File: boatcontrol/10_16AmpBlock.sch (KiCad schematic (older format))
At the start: 15 parts, among them U6101 ULN2803A

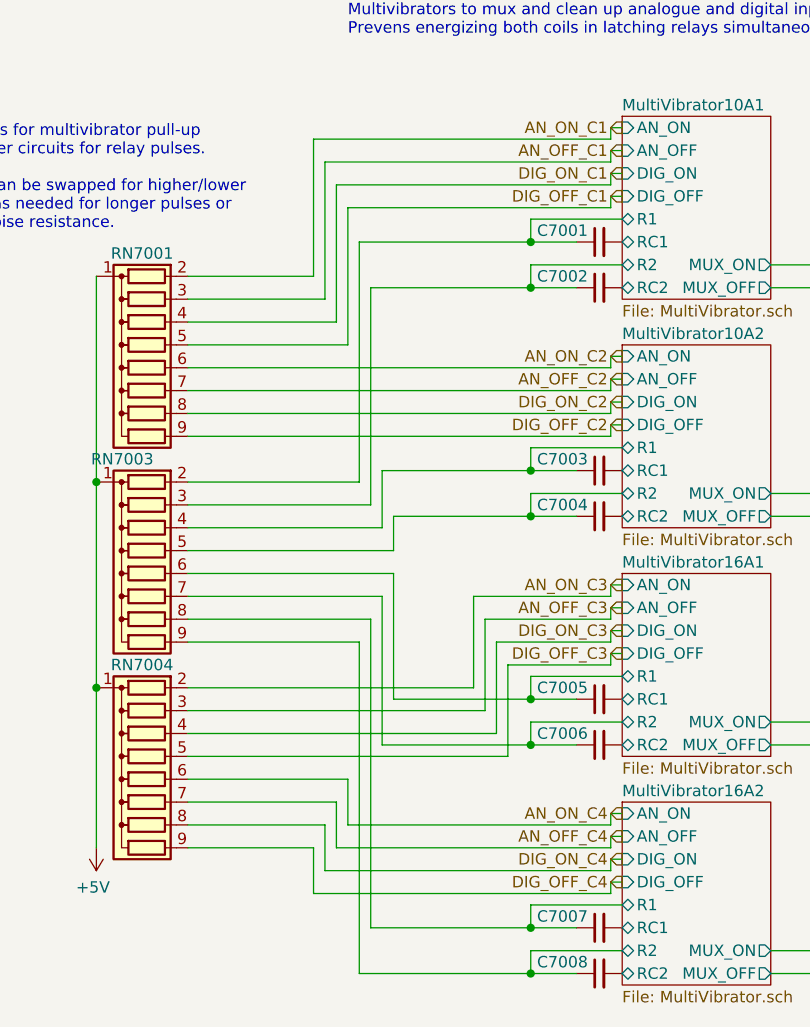
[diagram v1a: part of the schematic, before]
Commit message: Rewiring resistors done
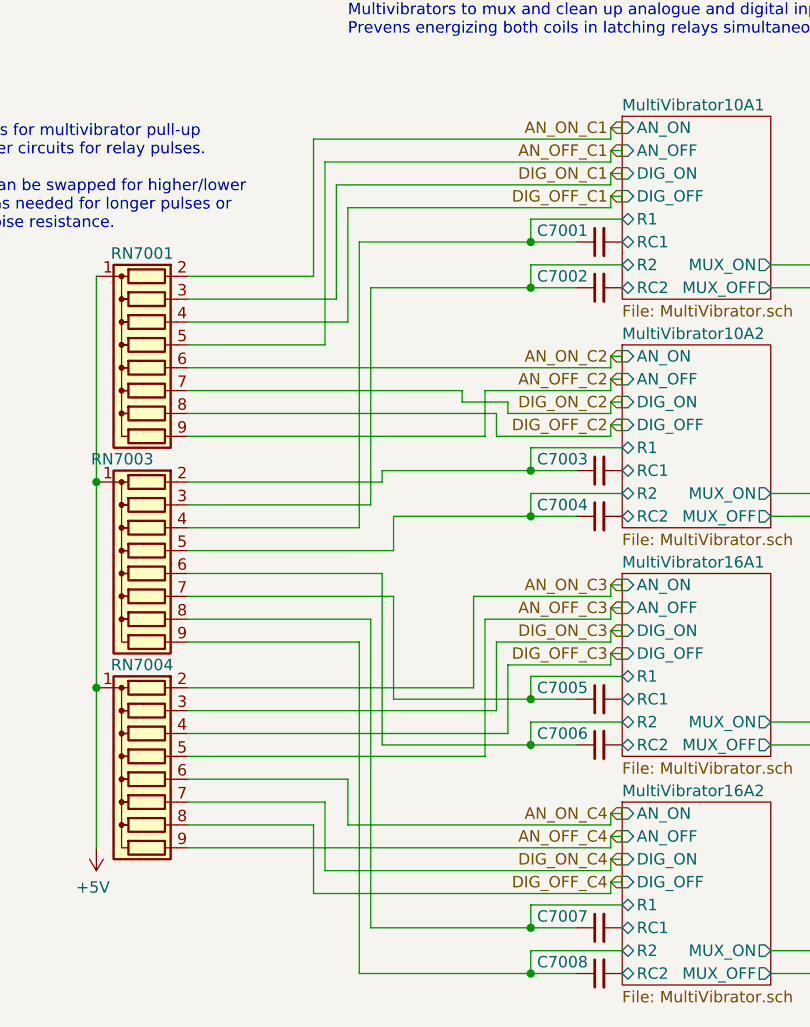
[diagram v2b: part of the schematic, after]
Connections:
- net AN_OFF_C1: now also RN6101.5 (R4); no longer RN6101.3 (R2)
- net AN_OFF_C2: now also RN6101.9 (R8); no longer RN6101.7 (R6)
- net AN_OFF_C3: now also RN6104.5 (R4); no longer RN6104.3 (R2)
- net AN_OFF_C4: now also RN6104.9 (R8); no longer RN6104.7 (R6)
- net DIG_OFF_C1: now also RN6101.4 (R3); no longer RN6101.5 (R4)
- net DIG_OFF_C2: now also RN6101.8 (R7); no longer RN6101.9 (R8)
- net DIG_OFF_C3: now also RN6104.4 (R3); no longer RN6104.5 (R4)
- net DIG_OFF_C4: now also RN6104.8 (R7); no longer RN6104.9 (R8)
- net DIG_ON_C1: now also RN6101.3 (R2); no longer RN6101.4 (R3)
- net DIG_ON_C2: now also RN6101.7 (R6); no longer RN6101.8 (R7)
- net DIG_ON_C3: now also RN6104.3 (R2); no longer RN6104.4 (R3)
- net DIG_ON_C4: now also RN6104.7 (R6); no longer RN6104.8 (R7)
- net MultiVibrator10A1/R1: now also RN7003.4 (R3); no longer RN7003.2 (R1)
- net MultiVibrator10A2/R1: now also RN7003.2 (R1); no longer RN7003.4 (R3)
- net MultiVibrator16A1/R1: now also RN7003.7 (R6); no longer RN7003.6 (R5)
- net MultiVibrator16A1/R2: now also RN7003.6 (R5); no longer RN7003.7 (R6)

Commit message: mwire
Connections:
- net 10AC1/OFF_COIL: now also RN6102.10 (R7.2); no longer RN6102.9 (R8.2)
- net 10AC1/ON_COIL: now also RN6102.9 (R8.2); no longer RN6102.10 (R7.2)
- net 10AC2/OFF_COIL: now also RN6102.12 (R5.2); no longer RN6102.11 (R6.2)
- net 10AC2/ON_COIL: now also RN6102.11 (R6.2); no longer RN6102.12 (R5.2)
- net 16AC1/OFF_COIL: now also RN6102.14 (R3.2); no longer RN6102.13 (R4.2)
- net 16AC1/ON_COIL: now also RN6102.13 (R4.2); no longer RN6102.14 (R3.2)
- net 16AC2/OFF_COIL: now also RN6102.16 (R1.2); no longer RN6102.15 (R2.2)
- net 16AC2/ON_COIL: now also RN6102.15 (R2.2); no longer RN6102.16 (R1.2)
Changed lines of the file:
@@
 $Descr A4 11693 8268
 encoding utf-8
-Sheet 69 97
+Sheet 49 97
 Title "Boat Control Hat"
 Date "2020-07-09"
@@
 AR Path="/D1BB8DB4/5F76AF55/604747AF" Ref="U6101"  Part="1"
 AR Path="/D1BB8DB4/5F75E923/604747AF" Ref="U7001"  Part="1"
-F 0 "U7001" H 6450 3500 50  0000 L CNN
+F 0 "U6101" H 6450 3500 50  0000 L CNN
 F 1 "ULN2803A" H 6300 4200 50  0000 L CNN
 F 2 "Package_DIP:DIP-18_W7.62mm" H 6550 3050 50  0001 L CNN
@@
 AR Path="/D1BB8DB4/5F76AF55/60474926" Ref="RN6102"  Part="1"
 AR Path="/D1BB8DB4/5F75E923/60474926" Ref="RN7002"  Part="1"
-F 0 "RN7002" V 10200 4350 50  0000 L CNN
+F 0 "RN6102" V 10200 4350 50  0000 L CNN
 F 1 "680Ω" V 9800 3750 50  0001 L CNN
 F 2 "BoatControl:DIP254P762X432-16P" V 10775 3900 50  0001 C CNN
@@
 AR Path="/D1BB8DB4/5F75E923/62B5C7B5" Ref="C7001"  Part="1"
 AR Path="/D1BB8DB4/5F76AF55/62B5C7B5" Ref="C6101"  Part="1"
-F 0 "C7001" V 4600 2550 50  0000 L CNN
+F 0 "C6101" V 4600 2550 50  0000 L CNN
 F 1 "1µF" H 3800 2400 50  0001 L CNN
 F 2 "Capacitor_THT:C_Disc_D7.5mm_W5.0mm_P5.00mm" H 4650 2500 50  0001 C CNN
@@
 AR Path="/D1BB8DB4/5F75E923/62B76848" Ref="C7002"  Part="1"
 AR Path="/D1BB8DB4/5F76AF55/62B76848" Ref="C6102"  Part="1"
-F 0 "C7002" V 4600 2750 50  0000 L CNN
+F 0 "C6102" V 4600 2750 50  0000 L CNN
 F 1 "1µF" H 3800 2600 50  0001 L CNN
 F 2 "Capacitor_THT:C_Disc_D7.5mm_W5.0mm_P5.00mm" H 4650 2700 50  0001 C CNN
@@
 AR Path="/D1BB8DB4/5F75E923/62B86A50" Ref="C7003"  Part="1"
 AR Path="/D1BB8DB4/5F76AF55/62B86A50" Ref="C6103"  Part="1"
-F 0 "C7003" V 4600 3550 50  0000 L CNN
+F 0 "C6103" V 4600 3550 50  0000 L CNN
 F 1 "1µF" H 3800 3400 50  0001 L CNN
 F 2 "Capacitor_THT:C_Disc_D7.5mm_W5.0mm_P5.00mm" H 4650 3500 50  0001 C CNN
@@
 AR Path="/D1BB8DB4/5F75E923/62B939DB" Ref="C7004"  Part="1"
 AR Path="/D1BB8DB4/5F76AF55/62B939DB" Ref="C6104"  Part="1"
-F 0 "C7004" V 4600 3750 50  0000 L CNN
+F 0 "C6104" V 4600 3750 50  0000 L CNN
 F 1 "1µF" H 3800 3600 50  0001 L CNN
 F 2 "Capacitor_THT:C_Disc_D7.5mm_W5.0mm_P5.00mm" H 4650 3700 50  0001 C CNN
@@
 AR Path="/D1BB8DB4/5F75E923/62BA14CE" Ref="C7005"  Part="1"
 AR Path="/D1BB8DB4/5F76AF55/62BA14CE" Ref="C6105"  Part="1"
-F 0 "C7005" V 4600 4550 50  0000 L CNN
+F 0 "C6105" V 4600 4550 50  0000 L CNN
 F 1 "1µF" H 3800 4400 50  0001 L CNN
 F 2 "Capacitor_THT:C_Disc_D7.5mm_W5.0mm_P5.00mm" H 4650 4500 50  0001 C CNN
@@
 AR Path="/D1BB8DB4/5F75E923/62BAE342" Ref="C7006"  Part="1"
 AR Path="/D1BB8DB4/5F76AF55/62BAE342" Ref="C6106"  Part="1"
-F 0 "C7006" V 4600 4750 50  0000 L CNN
+F 0 "C6106" V 4600 4750 50  0000 L CNN
 F 1 "1µF" H 3800 4600 50  0001 L CNN
 F 2 "Capacitor_THT:C_Disc_D7.5mm_W5.0mm_P5.00mm" H 4650 4700 50  0001 C CNN
@@
 AR Path="/D1BB8DB4/5F75E923/62BBBC28" Ref="C7007"  Part="1"
 AR Path="/D1BB8DB4/5F76AF55/62BBBC28" Ref="C6107"  Part="1"
-F 0 "C7007" V 4600 5550 50  0000 L CNN
+F 0 "C6107" V 4600 5550 50  0000 L CNN
 F 1 "1µF" H 3800 5400 50  0001 L CNN
 F 2 "Capacitor_THT:C_Disc_D7.5mm_W5.0mm_P5.00mm" H 4650 5500 50  0001 C CNN
@@
 AR Path="/D1BB8DB4/5F75E923/62BC8A92" Ref="C7008"  Part="1"
 AR Path="/D1BB8DB4/5F76AF55/62BC8A92" Ref="C6108"  Part="1"
-F 0 "C7008" V 4600 5750 50  0000 L CNN
+F 0 "C6108" V 4600 5750 50  0000 L CNN
 F 1 "1µF" H 3800 5600 50  0001 L CNN
 F 2 "Capacitor_THT:C_Disc_D7.5mm_W5.0mm_P5.00mm" H 4650 5700 50  0001 C CNN
@@
 AR Path="/D1BB8DB4/5F75E923/62CB5764" Ref="RN7003"  Part="1"
 AR Path="/D1BB8DB4/5F76AF55/62CB5764" Ref="RN6103"  Part="1"
-F 0 "RN7003" V 2150 3900 50  0000 L CNN
+F 0 "RN6103" V 2150 3900 50  0000 L CNN
 F 1 "10MΩ" H 2300 3550 50  0001 L CNN
 F 2 "Resistor_THT:R_Array_SIP9" V 3125 3950 50  0001 C CNN
@@
 AR Path="/D1BB8DB4/5F76AF55/630078FE" Ref="RN6101"  Part="1"
 AR Path="/D1BB8DB4/5F75E923/630078FE" Ref="RN7001"  Part="1"
-F 0 "RN7001" V 2150 3050 50  0000 C CNN
+F 0 "RN6101" V 2150 3050 50  0000 C CNN
 F 1 "100KΩ" V 2450 2750 50  0001 C CNN
 F 2 "Resistor_THT:R_Array_SIP9" H 3400 3150 50  0001 L CNN
@@
 AR Path="/D1BB8DB4/5F76AF55/63015012" Ref="RN6104"  Part="1"
 AR Path="/D1BB8DB4/5F75E923/63015012" Ref="RN7004"  Part="1"
-F 0 "RN7004" V 2150 4850 50  0000 C CNN
+F 0 "RN6104" V 2150 4850 50  0000 C CNN
 F 1 "100KΩ" V 2450 4550 50  0001 C CNN
 F 2 "Resistor_THT:R_Array_SIP9" H 3400 4950 50  0001 L CNN
@@
 	10650 3900 10650 4400
 Wire Wire Line
-	10500 3900 10650 3900
-Wire Wire Line
 	9550 4350 9900 4350
 Wire Wire Line
@@
 	10600 4000 10600 4300
 Wire Wire Line
-	10500 4000 10600 4000
-Wire Wire Line
 	10550 5050 9550 5050
 Wire Wire Line
 	10550 4100 10550 5050
 Wire Wire Line
-	10500 4100 10550 4100
-Wire Wire Line
 	9550 4950 10500 4950
 Wire Wire Line
-	10500 4200 10500 4950
-Wire Wire Line
 	9900 3900 10100 3900
 Wire Wire Line
@@
 	10700 3800 10700 3150
 Wire Wire Line
-	10500 3800 10700 3800
-Wire Wire Line
 	10650 3250 10650 3700
 Wire Wire Line
@@
 	9550 3450 9950 3450
 Wire Wire Line
-	10600 2250 10600 3600
-Wire Wire Line
 	10600 2250 9550 2250
 Wire Wire Line
-	10500 3700 10650 3700
-Wire Wire Line
 	9900 3800 10100 3800
 Wire Wire Line
@@
 Wire Wire Line
 	10050 3500 10100 3500
-Wire Wire Line
-	10500 3600 10600 3600
-Wire Wire Line
-	10550 3500 10500 3500
-Wire Wire Line
-	10550 2350 10550 3500
 Wire Wire Line
 	9550 2350 10550 2350
@@
 F6 "OUT" O R 9550 5500 50
 F7 "IN" I L 8550 5500 50
-F8 "ON_COIL" I R 9550 5050 50
-F9 "OFF_COIL" I R 9550 4950 50
+F8 "ON_COIL" I R 9550 4950 50
+F9 "OFF_COIL" I R 9550 5050 50
 $EndSheet
 Wire Wire Line
@@
 F6 "OUT" O R 9550 3700 50
 F7 "IN" I L 8550 3700 50
-F8 "ON_COIL" I R 9550 3250 50
-F9 "OFF_COIL" I R 9550 3150 50
+F8 "ON_COIL" I R 9550 3150 50
+F9 "OFF_COIL" I R 9550 3250 50
 $EndSheet
 $Sheet
@@
 F6 "OUT" O R 9550 2800 50
 F7 "IN" I L 8550 2800 50
-F8 "ON_COIL" I R 9550 2350 50
-F9 "OFF_COIL" I R 9550 2250 50
+F8 "ON_COIL" I R 9550 2250 50
+F9 "OFF_COIL" I R 9550 2350 50
 $EndSheet
 $Sheet
@@
 F6 "OUT" O R 9550 4600 50
 F7 "IN" I L 8550 4600 50
-F8 "ON_COIL" I R 9550 4150 50
-F9 "OFF_COIL" I R 9550 4050 50
+F8 "ON_COIL" I R 9550 4050 50
+F9 "OFF_COIL" I R 9550 4150 50
 $EndSheet
 $Comp
@@
 AR Path="/D1BB8DB4/5F76AF55/62505F9A" Ref="C6109"  Part="1"
 AR Path="/D1BB8DB4/5F75E923/62505F9A" Ref="C7009"  Part="1"
-F 0 "C7009" H 6300 2750 50  0000 L CNN
+F 0 "C6109" H 6300 2750 50  0000 L CNN
 F 1 "10uF" H 6491 2905 50  0001 L CNN
 F 2 "Capacitor_THT:C_Disc_D7.5mm_W5.0mm_P5.00mm" H 6400 2950 50  0001 C CNN
@@
 AR Path="/D1BB8DB4/5F76AF55/62505FA2" Ref="C6110"  Part="1"
 AR Path="/D1BB8DB4/5F75E923/62505FA2" Ref="C7010"  Part="1"
-F 0 "C7010" H 6550 2750 50  0000 L CNN
+F 0 "C6110" H 6550 2750 50  0000 L CNN
 F 1 "0.1uF" H 6741 2905 50  0001 L CNN
 F 2 "Capacitor_THT:C_Disc_D7.5mm_W5.0mm_P5.00mm" H 6650 2950 50  0001 C CNN
@@
 Wire Wire Line
 	3550 5050 4700 5050
+Wire Wire Line
+	10600 2250 10600 3600
+Wire Wire Line
+	10550 2350 10550 3500
+Wire Wire Line
+	10500 4200 10500 4950
+Wire Wire Line
+	10500 4100 10550 4100
+Wire Wire Line
+	10500 4000 10600 4000
+Wire Wire Line
+	10500 3900 10650 3900
+Wire Wire Line
+	10550 3500 10500 3500
+Wire Wire Line
+	10500 3600 10600 3600
+Wire Wire Line
+	10500 3700 10650 3700
+Wire Wire Line
+	10500 3800 10700 3800
 $EndSCHEMATC

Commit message: More cleanup
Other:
- moved on the sheet: RN6102

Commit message: More cleanup
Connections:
- net +5V: no longer RN6101.1 (common), RN6104.1 (common)
- net GND: now also RN6101.1 (common), RN6104.1 (common)
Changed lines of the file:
@@
 $Descr A4 11693 8268
 encoding utf-8
-Sheet 49 97
+Sheet 58 97
 Title "Boat Control Hat"
 Date "2020-07-09"
@@
 AR Path="/D1BB8DB4/5F76AF55/604747A2" Ref="#PWR06101"  Part="1"
 AR Path="/D1BB8DB4/5F75E923/604747A2" Ref="#PWR07001"  Part="1"
-F 0 "#PWR06101" H 6900 3250 50  0001 C CNN
+F 0 "#PWR07001" H 6900 3250 50  0001 C CNN
 F 1 "+12P" H 6750 3500 50  0000 C CNN
 F 2 "" H 6900 3400 50  0001 C CNN
@@
 AR Path="/D1BB8DB4/5F76AF55/604747AF" Ref="U6101"  Part="1"
 AR Path="/D1BB8DB4/5F75E923/604747AF" Ref="U7001"  Part="1"
-F 0 "U6101" H 6450 3500 50  0000 L CNN
+F 0 "U7001" H 6450 3500 50  0000 L CNN
 F 1 "ULN2803A" H 6300 4200 50  0000 L CNN
 F 2 "Package_DIP:DIP-18_W7.62mm" H 6550 3050 50  0001 L CNN
@@
 AR Path="/D1BB8DB4/5F76AF55/604747C1" Ref="#PWR06102"  Part="1"
 AR Path="/D1BB8DB4/5F75E923/604747C1" Ref="#PWR07002"  Part="1"
-F 0 "#PWR06102" H 6500 4150 50  0001 C CNN
+F 0 "#PWR07002" H 6500 4150 50  0001 C CNN
 F 1 "GND" H 6505 4227 50  0000 C CNN
 F 2 "" H 6500 4400 50  0001 C CNN
@@
 Wire Wire Line
 	5900 3900 6100 3900
-$Comp
-L power:+5V #PWR?
-U 1 1 6047484A
-P 2450 5150
-AR Path="/D16552B4/5FA17F38/6047484A" Ref="#PWR?"  Part="1"
-AR Path="/D16552B4/5FA17F52/6047484A" Ref="#PWR?"  Part="1"
-AR Path="/D16552B4/5FA17F6C/6047484A" Ref="#PWR?"  Part="1"
-AR Path="/D16552B4/5FA17F86/6047484A" Ref="#PWR?"  Part="1"
-AR Path="/D1BB8DB4/5F76AF55/6047484A" Ref="#PWR06103"  Part="1"
-AR Path="/D1BB8DB4/5F75E923/6047484A" Ref="#PWR07003"  Part="1"
-F 0 "#PWR06103" H 2450 5000 50  0001 C CNN
-F 1 "+5V" H 2465 5323 50  0000 C CNN
-F 2 "" H 2450 5150 50  0001 C CNN
-F 3 "" H 2450 5150 50  0001 C CNN
-	1    2450 5150
-	-1   0    0    1
-$EndComp
 Wire Wire Line
 	6900 3700 7150 3700
@@
 AR Path="/D1BB8DB4/5F76AF55/60474926" Ref="RN6102"  Part="1"
 AR Path="/D1BB8DB4/5F75E923/60474926" Ref="RN7002"  Part="1"
-F 0 "RN6102" V 10200 4250 50  0000 L CNN
+F 0 "RN7002" V 10200 4250 50  0000 L CNN
 F 1 "680Ω" V 9800 3650 50  0001 L CNN
 F 2 "BoatControl:DIP254P762X432-16P" V 10775 3800 50  0001 C CNN
@@
 AR Path="/D1BB8DB4/5F75E923/62B5C7B5" Ref="C7001"  Part="1"
 AR Path="/D1BB8DB4/5F76AF55/62B5C7B5" Ref="C6101"  Part="1"
-F 0 "C6101" V 4600 2550 50  0000 L CNN
+F 0 "C7001" V 4600 2550 50  0000 L CNN
 F 1 "1µF" H 3800 2400 50  0001 L CNN
 F 2 "Capacitor_THT:C_Disc_D7.5mm_W5.0mm_P5.00mm" H 4650 2500 50  0001 C CNN
@@
 AR Path="/D1BB8DB4/5F75E923/62B76848" Ref="C7002"  Part="1"
 AR Path="/D1BB8DB4/5F76AF55/62B76848" Ref="C6102"  Part="1"
-F 0 "C6102" V 4600 2750 50  0000 L CNN
+F 0 "C7002" V 4600 2750 50  0000 L CNN
 F 1 "1µF" H 3800 2600 50  0001 L CNN
 F 2 "Capacitor_THT:C_Disc_D7.5mm_W5.0mm_P5.00mm" H 4650 2700 50  0001 C CNN
@@
 AR Path="/D1BB8DB4/5F75E923/62B86A50" Ref="C7003"  Part="1"
 AR Path="/D1BB8DB4/5F76AF55/62B86A50" Ref="C6103"  Part="1"
-F 0 "C6103" V 4600 3550 50  0000 L CNN
+F 0 "C7003" V 4600 3550 50  0000 L CNN
 F 1 "1µF" H 3800 3400 50  0001 L CNN
 F 2 "Capacitor_THT:C_Disc_D7.5mm_W5.0mm_P5.00mm" H 4650 3500 50  0001 C CNN
@@
 AR Path="/D1BB8DB4/5F75E923/62B939DB" Ref="C7004"  Part="1"
 AR Path="/D1BB8DB4/5F76AF55/62B939DB" Ref="C6104"  Part="1"
-F 0 "C6104" V 4600 3750 50  0000 L CNN
+F 0 "C7004" V 4600 3750 50  0000 L CNN
 F 1 "1µF" H 3800 3600 50  0001 L CNN
 F 2 "Capacitor_THT:C_Disc_D7.5mm_W5.0mm_P5.00mm" H 4650 3700 50  0001 C CNN
@@
 AR Path="/D1BB8DB4/5F75E923/62BA14CE" Ref="C7005"  Part="1"
 AR Path="/D1BB8DB4/5F76AF55/62BA14CE" Ref="C6105"  Part="1"
-F 0 "C6105" V 4600 4550 50  0000 L CNN
+F 0 "C7005" V 4600 4550 50  0000 L CNN
 F 1 "1µF" H 3800 4400 50  0001 L CNN
 F 2 "Capacitor_THT:C_Disc_D7.5mm_W5.0mm_P5.00mm" H 4650 4500 50  0001 C CNN
@@
 AR Path="/D1BB8DB4/5F75E923/62BAE342" Ref="C7006"  Part="1"
 AR Path="/D1BB8DB4/5F76AF55/62BAE342" Ref="C6106"  Part="1"
-F 0 "C6106" V 4600 4750 50  0000 L CNN
+F 0 "C7006" V 4600 4750 50  0000 L CNN
 F 1 "1µF" H 3800 4600 50  0001 L CNN
 F 2 "Capacitor_THT:C_Disc_D7.5mm_W5.0mm_P5.00mm" H 4650 4700 50  0001 C CNN
@@
 AR Path="/D1BB8DB4/5F75E923/62BBBC28" Ref="C7007"  Part="1"
 AR Path="/D1BB8DB4/5F76AF55/62BBBC28" Ref="C6107"  Part="1"
-F 0 "C6107" V 4600 5550 50  0000 L CNN
+F 0 "C7007" V 4600 5550 50  0000 L CNN
 F 1 "1µF" H 3800 5400 50  0001 L CNN
 F 2 "Capacitor_THT:C_Disc_D7.5mm_W5.0mm_P5.00mm" H 4650 5500 50  0001 C CNN
@@
 AR Path="/D1BB8DB4/5F75E923/62BC8A92" Ref="C7008"  Part="1"
 AR Path="/D1BB8DB4/5F76AF55/62BC8A92" Ref="C6108"  Part="1"
-F 0 "C6108" V 4600 5750 50  0000 L CNN
+F 0 "C7008" V 4600 5750 50  0000 L CNN
 F 1 "1µF" H 3800 5600 50  0001 L CNN
 F 2 "Capacitor_THT:C_Disc_D7.5mm_W5.0mm_P5.00mm" H 4650 5700 50  0001 C CNN
@@
 AR Path="/D1BB8DB4/5F75E923/62CB5764" Ref="RN7003"  Part="1"
 AR Path="/D1BB8DB4/5F76AF55/62CB5764" Ref="RN6103"  Part="1"
-F 0 "RN6103" V 2150 3900 50  0000 L CNN
+F 0 "RN7003" V 2150 3900 50  0000 L CNN
 F 1 "10MΩ" H 2300 3550 50  0001 L CNN
 F 2 "Resistor_THT:R_Array_SIP9" V 3125 3950 50  0001 C CNN
@@
 	0    -1   1    0
 $EndComp
-Connection ~ 2450 3550
-Wire Wire Line
-	2450 2650 2450 3550
 $Comp
 L Device:R_Network08 RN?
@@
 AR Path="/D1BB8DB4/5F76AF55/630078FE" Ref="RN6101"  Part="1"
 AR Path="/D1BB8DB4/5F75E923/630078FE" Ref="RN7001"  Part="1"
-F 0 "RN6101" V 2150 3050 50  0000 C CNN
+F 0 "RN7001" V 2150 3050 50  0000 C CNN
 F 1 "100KΩ" V 2450 2750 50  0001 C CNN
 F 2 "Resistor_THT:R_Array_SIP9" H 3400 3150 50  0001 L CNN
@@
 	0    -1   1    0
 $EndComp
-Wire Wire Line
-	2450 3550 2450 4450
 $Comp
 L Device:R_Network08 RN?
@@
 AR Path="/D1BB8DB4/5F76AF55/63015012" Ref="RN6104"  Part="1"
 AR Path="/D1BB8DB4/5F75E923/63015012" Ref="RN7004"  Part="1"
-F 0 "RN6104" V 2150 4850 50  0000 C CNN
+F 0 "RN7004" V 2150 4850 50  0000 C CNN
 F 1 "100KΩ" V 2450 4550 50  0001 C CNN
 F 2 "Resistor_THT:R_Array_SIP9" H 3400 4950 50  0001 L CNN
@@
 	0    -1   1    0
 $EndComp
-Connection ~ 2450 4450
-Wire Wire Line
-	2450 4450 2450 5150
 Wire Wire Line
 	9850 4200 9850 3950
@@
 AR Path="/D1BB8DB4/5F76AF55/62505F9A" Ref="C6109"  Part="1"
 AR Path="/D1BB8DB4/5F75E923/62505F9A" Ref="C7009"  Part="1"
-F 0 "C6109" H 6300 2750 50  0000 L CNN
+F 0 "C7009" H 6300 2750 50  0000 L CNN
 F 1 "10uF" H 6491 2905 50  0001 L CNN
 F 2 "Capacitor_THT:C_Disc_D7.5mm_W5.0mm_P5.00mm" H 6400 2950 50  0001 C CNN
@@
 AR Path="/D1BB8DB4/5F76AF55/62505FA2" Ref="C6110"  Part="1"
 AR Path="/D1BB8DB4/5F75E923/62505FA2" Ref="C7010"  Part="1"
-F 0 "C6110" H 6550 2750 50  0000 L CNN
+F 0 "C7010" H 6550 2750 50  0000 L CNN
 F 1 "0.1uF" H 6741 2905 50  0001 L CNN
 F 2 "Capacitor_THT:C_Disc_D7.5mm_W5.0mm_P5.00mm" H 6650 2950 50  0001 C CNN
@@
 AR Path="/D1BB8DB4/5F75E923/62505FA9" Ref="#PWR0200"  Part="1"
 AR Path="/D1BB8DB4/5F76AF55/62505FA9" Ref="#PWR0199"  Part="1"
-F 0 "#PWR0199" H 6650 2600 50  0001 C CNN
+F 0 "#PWR0200" H 6650 2600 50  0001 C CNN
 F 1 "GND" V 6655 2722 50  0000 R CNN
 F 2 "" H 6650 2850 50  0001 C CNN
@@
 Wire Wire Line
 	7050 4900 8550 4900
+$Comp
+L power:+5V #PWR?
+U 1 1 602F484F
+P 2450 3550
+AR Path="/D16552B4/5FA17F38/602F484F" Ref="#PWR?"  Part="1"
+AR Path="/D16552B4/5FA17F52/602F484F" Ref="#PWR?"  Part="1"
+AR Path="/D16552B4/5FA17F6C/602F484F" Ref="#PWR?"  Part="1"
+AR Path="/D16552B4/5FA17F86/602F484F" Ref="#PWR?"  Part="1"
+AR Path="/D1BB8DB4/5F75E923/602F484F" Ref="#PWR?"  Part="1"
+F 0 "#PWR?" H 2450 3400 50  0001 C CNN
+F 1 "+5V" H 2600 3600 50  0000 C CNN
+F 2 "" H 2450 3550 50  0001 C CNN
+F 3 "" H 2450 3550 50  0001 C CNN
+	1    2450 3550
+	-1   0    0    1
+$EndComp
+$Comp
+L power:GND #PWR?
+U 1 1 602F4855
+P 2450 2650
+AR Path="/D16552B4/5FA17F38/602F4855" Ref="#PWR?"  Part="1"
+AR Path="/D1BB8DB4/5F75E923/602F4855" Ref="#PWR?"  Part="1"
+F 0 "#PWR?" H 2450 2400 50  0001 C CNN
+F 1 "GND" H 2300 2600 50  0000 C CNN
+F 2 "" H 2450 2650 50  0001 C CNN
+F 3 "" H 2450 2650 50  0001 C CNN
+	1    2450 2650
+	1    0    0    -1
+$EndComp
+$Comp
+L power:GND #PWR?
+U 1 1 602F485B
+P 2450 4450
+AR Path="/D16552B4/5FA17F38/602F485B" Ref="#PWR?"  Part="1"
+AR Path="/D1BB8DB4/5F75E923/602F485B" Ref="#PWR?"  Part="1"
+F 0 "#PWR?" H 2450 4200 50  0001 C CNN
+F 1 "GND" H 2300 4400 50  0000 C CNN
+F 2 "" H 2450 4450 50  0001 C CNN
+F 3 "" H 2450 4450 50  0001 C CNN
+	1    2450 4450
+	1    0    0    -1
+$EndComp
 $EndSCHEMATC
